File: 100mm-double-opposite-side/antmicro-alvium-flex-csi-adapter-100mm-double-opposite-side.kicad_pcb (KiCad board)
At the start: 2 copper layers, 81.8 x 100.1 mm, 4 parts, among them J1 WE_687622100002_FLEX, J2 WE_687622100002_FLEX, J3 WE_687650100002_FLEX

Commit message: 100mm-double-same: Add signage
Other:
- board text added: "Antmicro Alvium Flex CSI Adapter 100mm double opposite side contacts Rev. 1.0.0"
- board text removed: "Antmicro Alvium Flex CSI Adapter 100mm double opposite contacts Rev. 1.0.0"
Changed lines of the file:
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@@
   (gr_line (start 158.54 106.55) (end 158.54 107.65) (layer B.SilkS) (width 0.12))
   (gr_circle (center 158.52 105.98) (end 158.18 106.41) (layer B.SilkS) (width 0.12))
-  (gr_text "Antmicro Alvium\nFlex CSI Adapter\n100mm double\nopposite contacts\nRev. 1.0.0" (at 88.28 86.98 270) (layer B.SilkS)
+  (gr_text "Antmicro Alvium\nFlex CSI Adapter\n100mm double\nopposite side contacts\nRev. 1.0.0" (at 88.28 86.98 270) (layer B.SilkS)
     (effects (font (size 1 1) (thickness 0.15)) (justify left mirror))
   )

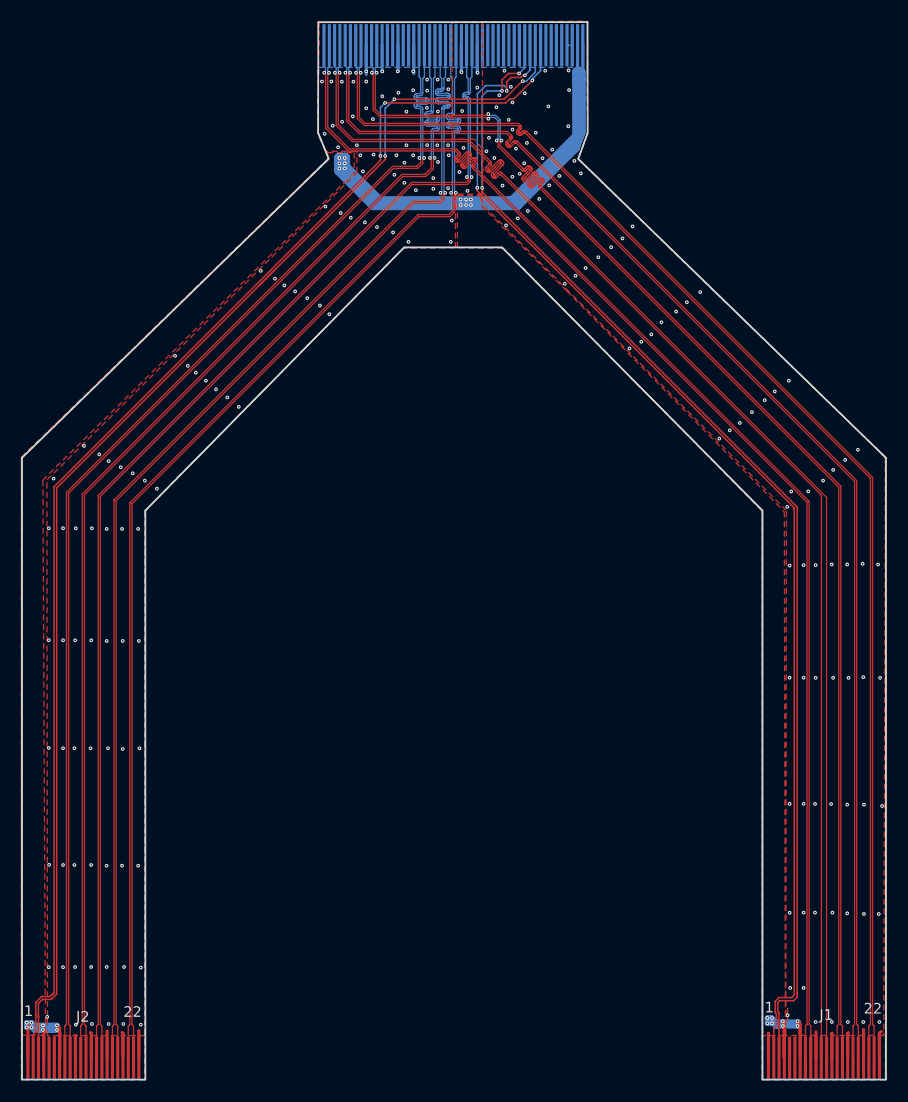
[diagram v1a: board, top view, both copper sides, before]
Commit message: Add NMOS transistors for camera triggering in 100mm double opposite side variant
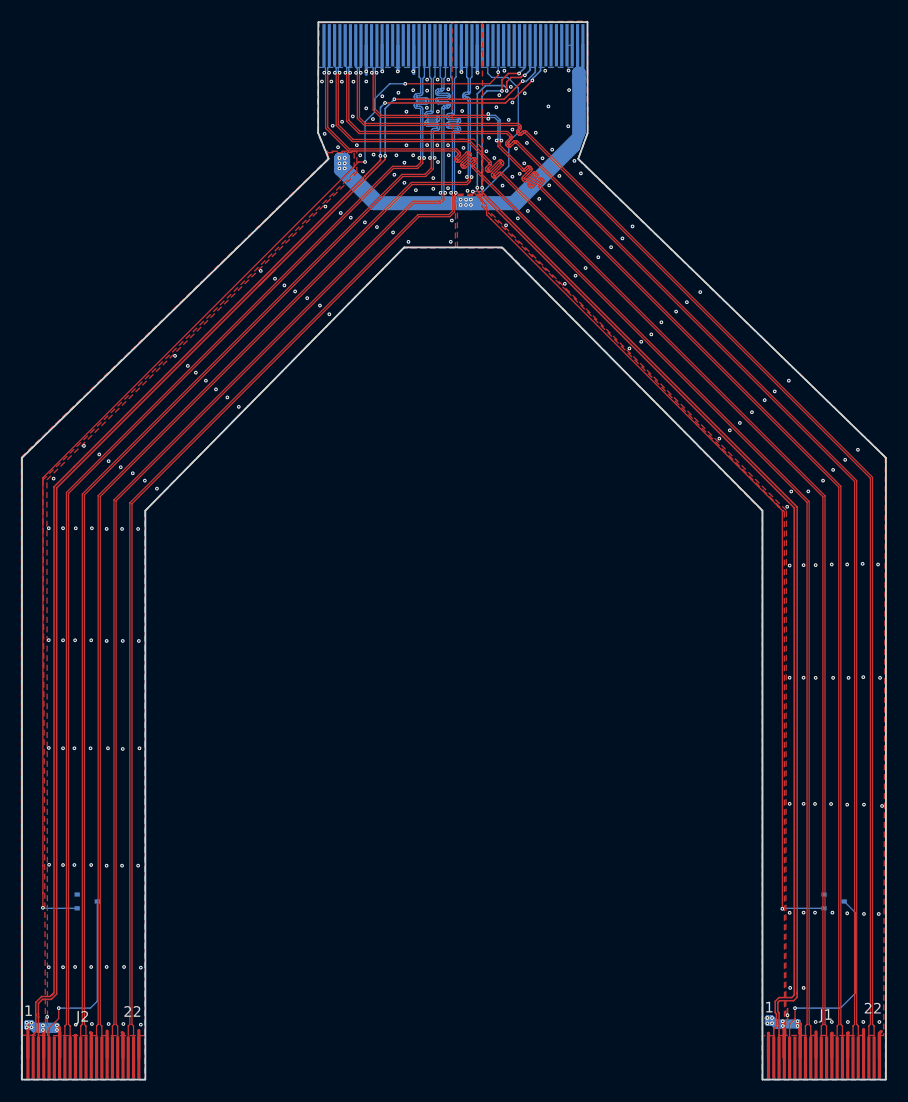
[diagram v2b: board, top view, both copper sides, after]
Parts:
- added Q1: BSS138APW, antmicro-alvium-flex-csi-adapter-footprints:SC70-3, B.Cu at (159.1, 102.0)
- added Q2: BSS138APW, antmicro-alvium-flex-csi-adapter-footprints:SC70-3, B.Cu at (88.4, 102.0)
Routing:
- net /F1_C2_VSYNC: track 0.00 -> 108.7 mm, vias 0 -> 4
- net /F1_C1_VSYNC: track 0.00 -> 102.4 mm, vias 0 -> 2
- net /F1_C1_GPIO2: track 0.00 -> 20.3 mm, vias 0 -> 1
- net /F1_C2_GPIO2: track 0.00 -> 18.4 mm, vias 0 -> 1
